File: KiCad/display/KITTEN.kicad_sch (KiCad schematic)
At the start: 19 parts, among them J1 Barrel_Jack_Switch, J10 Conn_01x02_Pin, J2 Conn_01x03_Pin, J3 Conn_01x04_Pin, J4 Conn_01x05_Pin, J5 Conn_01x06_Pin, J6 Conn_01x07_Pin, J7 Conn_01x08_Pin, J8 Conn_01x09_Pin, J9 Conn_01x10_Pin, SW1 Cherry Switch Single, SW2 Cherry Switch 1.5x - Enter Key, U2 TMC2209, U3 Display, U4 ICM-20948, U5 24LC512, U6 Adafruit_ICM20948, U7 LTV-817S

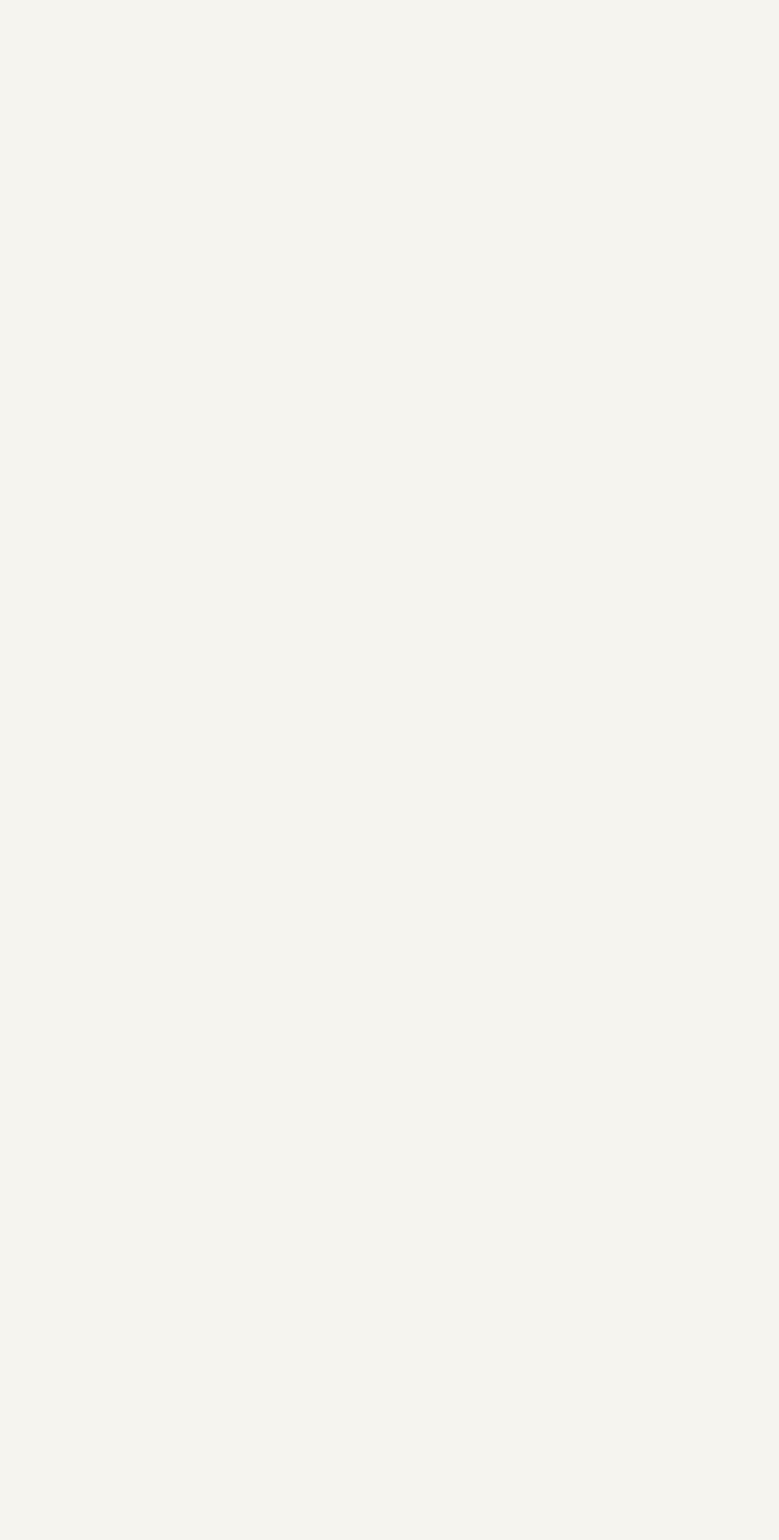
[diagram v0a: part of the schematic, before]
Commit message: numpad schematic started
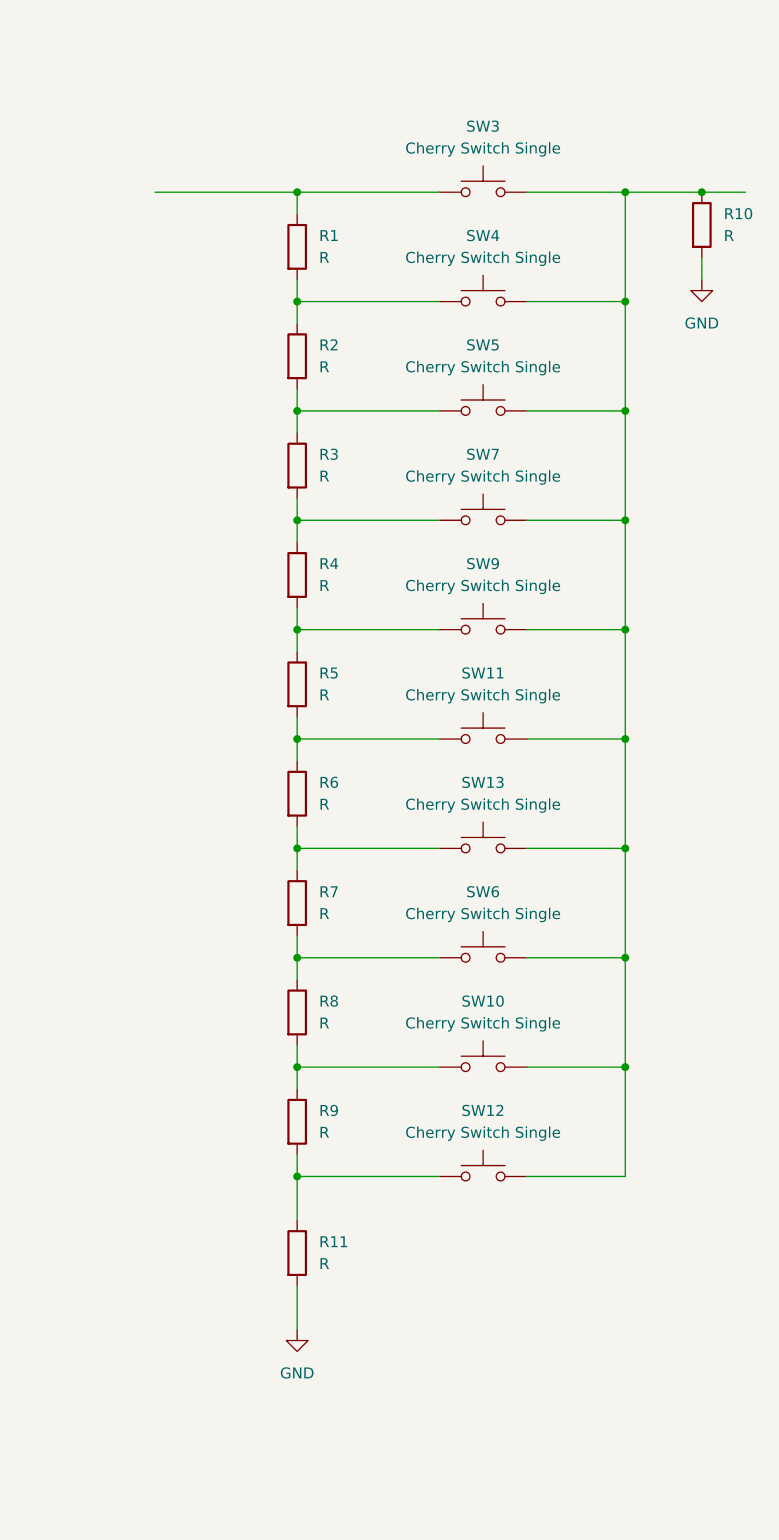
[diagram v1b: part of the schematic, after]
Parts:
- added R1, R10, R11, R2, R3, R4, R5, R6, R7, R8, R9: R, Resistor_SMD:R_0603_1608Metric, symbol Device:R
- added SW10, SW11, SW12, SW13, SW3, SW4, SW5, SW6, SW7, SW9: Cherry Switch Single, ComponentLib:SW_Cherry_MX_1.00u_PCB, symbol Switch:SW_Push
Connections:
- new net: R5.2, R6.1, SW11.1
- new net: R6.2, R7.1, SW13.1
- new net: R7.2, R8.1, SW6.1
- new net: R10.1, SW10.2, SW11.2, SW12.2, SW13.2, SW3.2, SW4.2, SW5.2, SW6.2, SW7.2, SW9.2
- new net: R8.2, R9.1, SW10.1
- new net: R11.1, R9.2, SW12.1
- new net: R3.2, R4.1, SW7.1
- new net: R4.2, R5.1, SW9.1
- new net: R1.1, SW3.1
- new net: R1.2, R2.1, SW4.1
- new net: R2.2, R3.1, SW5.1
- new net GND: R10.2, R11.2

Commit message: Display and numpad schematics
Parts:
- removed J1: Barrel_Jack_Switch, Connector_BarrelJack:BarrelJack_Wuerth_694106106102_2.0x5.5mm, symbol Connector:Barrel_Jack_Switch
- removed J10: Conn_01x02_Pin, Connector_JST:JST_PH_B2B-PH-K_1x02_P2.00mm_Vertical, symbol Connector:Conn_01x02_Pin
- removed J2: Conn_01x03_Pin, Connector_JST:JST_PH_B3B-PH-K_1x03_P2.00mm_Vertical, symbol Connector:Conn_01x03_Pin
- removed J3: Conn_01x04_Pin, Connector_JST:JST_PH_B4B-PH-K_1x04_P2.00mm_Vertical, symbol Connector:Conn_01x04_Pin
- removed J5: Conn_01x06_Pin, Connector_JST:JST_PH_B6B-PH-K_1x06_P2.00mm_Vertical, symbol Connector:Conn_01x06_Pin
- removed J6: Conn_01x07_Pin, Connector_JST:JST_PH_B7B-PH-K_1x07_P2.00mm_Vertical, symbol Connector:Conn_01x07_Pin
- removed J7: Conn_01x08_Pin, Connector_JST:JST_PH_B8B-PH-K_1x08_P2.00mm_Vertical, symbol Connector:Conn_01x08_Pin
- removed J8: Conn_01x09_Pin, Connector_JST:JST_PH_B9B-PH-K_1x09_P2.00mm_Vertical, symbol Connector:Conn_01x09_Pin
- removed J9: Conn_01x10_Pin, Connector_JST:JST_PH_B10B-PH-K_1x10_P2.00mm_Vertical, symbol Connector:Conn_01x10_Pin
- removed R10, R11, R5, R6, R7, R8, R9: R, Resistor_SMD:R_0603_1608Metric, symbol Device:R
- removed SW1, SW10, SW11, SW12, SW13, SW3, SW4, SW5, SW6, SW7, SW9: Cherry Switch Single, ComponentLib:SW_Cherry_MX_1.00u_PCB, symbol Switch:SW_Push
- removed SW2: Cherry Switch 1.5x - Enter Key, ComponentLib:SW_Cherry_MX_1.50u_PCB, symbol Switch:SW_Push
- removed U1: ~, ComponentLib:NUCLEO-F767ZI, symbol SymbolLib:NUCLEO-F767ZI
- removed U2: TMC2209, ComponentLib:TMC2209 Silentstepstick, symbol SymbolLib:TMC2209_Silentstepstick
- removed U4: ICM-20948, ComponentLib:ICM-20948, symbol Sensor_Motion:ICM-20948
- removed U5: 24LC512, Package_SO:SOIC-8_5.3x6.2mm_P1.27mm, symbol Memory_EEPROM:24LC512
- removed U6: Adafruit_ICM20948, ComponentLib:Adafruit-ICM-20948, symbol SymbolLib:Adafruit_ICM20948
- removed U7: LTV-817S, Package_DIP:SMDIP-4_W9.53mm, symbol Isolator:LTV-817S
- added D1: LED, Diode_SMD:D_0603_1608Metric, symbol Device:LED
- added JP1: SolderJumper_2_Open, Resistor_SMD:R_0603_1608Metric_Pad0.98x0.95mm_HandSolder, symbol Jumper:SolderJumper_2_Open
- R1, R2: value R -> 2k
- R3: value R -> 150R
- R4: value R -> 15k; footprint Resistor_SMD:R_0603_1608Metric -> Resistor_SMD:R_0603_1608Metric_Pad0.98x0.95mm_HandSolder
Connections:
- net GND: now also J4.4 (Pin_4), R4.2, U3.1 (VSS), U3.10 (D3), U3.11 (D4), U3.12 (D5), U3.13 (D6), U3.14 (D7), U3.17 (~{CS}), U3.19 (BS2), U3.5 (WR), U3.6 (RD), D1.1 (K)
- net ~{RES}: now reaches U3.16 (~{RES})
- net ~{RES}: now also J4.5 (Pin_5)
- net +3V3: now reaches U3.2 (VDD)
- net +3V3: now also J4.3 (Pin_3), R1.1, R2.1, R3.1, U3.20 (BS1), JP1.2 (B)
- net A0: now reaches U3.4 (D~{C})
- net A0: now also R4.1, JP1.1 (A)
- net SCL: now reaches U3.7 (D0)
- net SCL: now also J4.1 (Pin_1), R1.2
- net SDA: now reaches U3.8 (D1)
- net SDA: now also J4.2 (Pin_2), R2.2, U3.9 (D2)
- net at R3.2: now also D1.2 (A); no longer R4.1
- no-connect marks 0 -> 7
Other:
- note added: "A0 low (JP0 open) : addr = 0b0111100 A0 high (JP0 closed): addr = 0b0111101"
- note added: "Csatlakozó"
- note added: "I2C address A0"
- note added: "Kijelző"
- note added: "Visszajelző LED"
- moved on the sheet: J4, U3
